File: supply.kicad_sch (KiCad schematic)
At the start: 0 parts

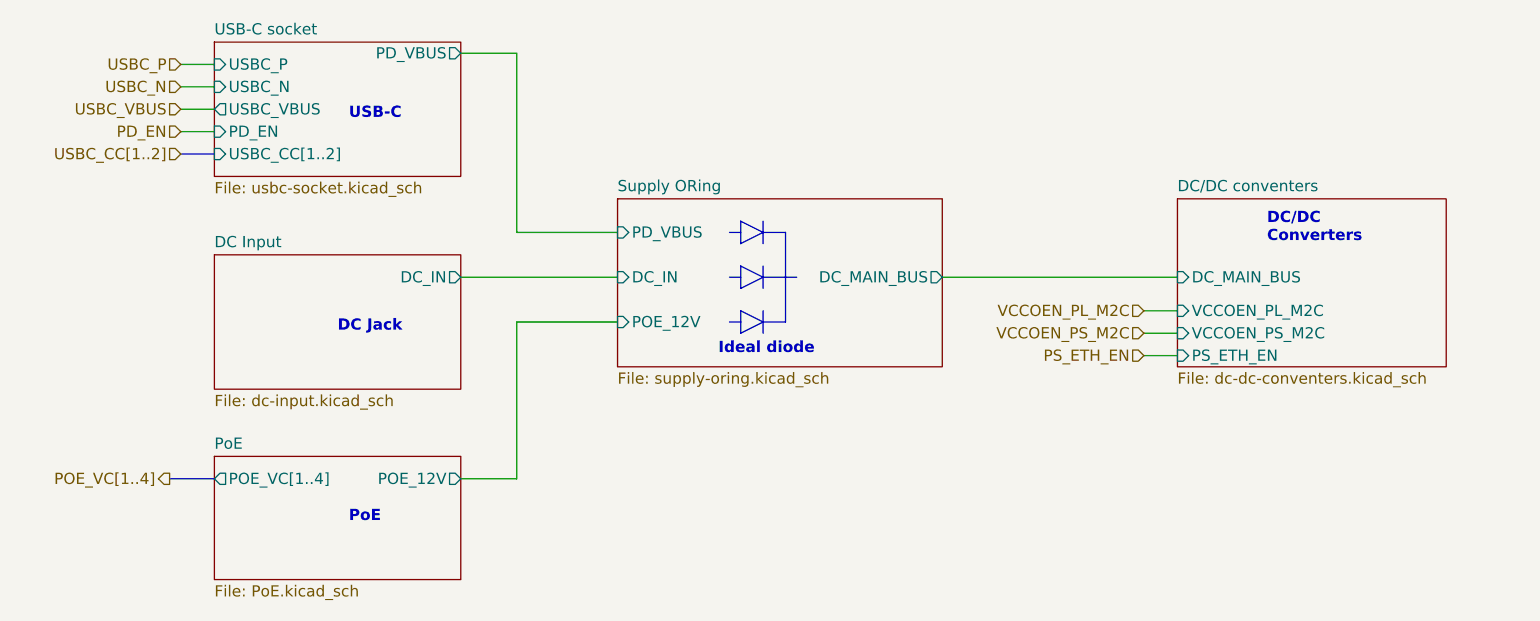
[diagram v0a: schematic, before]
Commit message: removed PoE from schematic
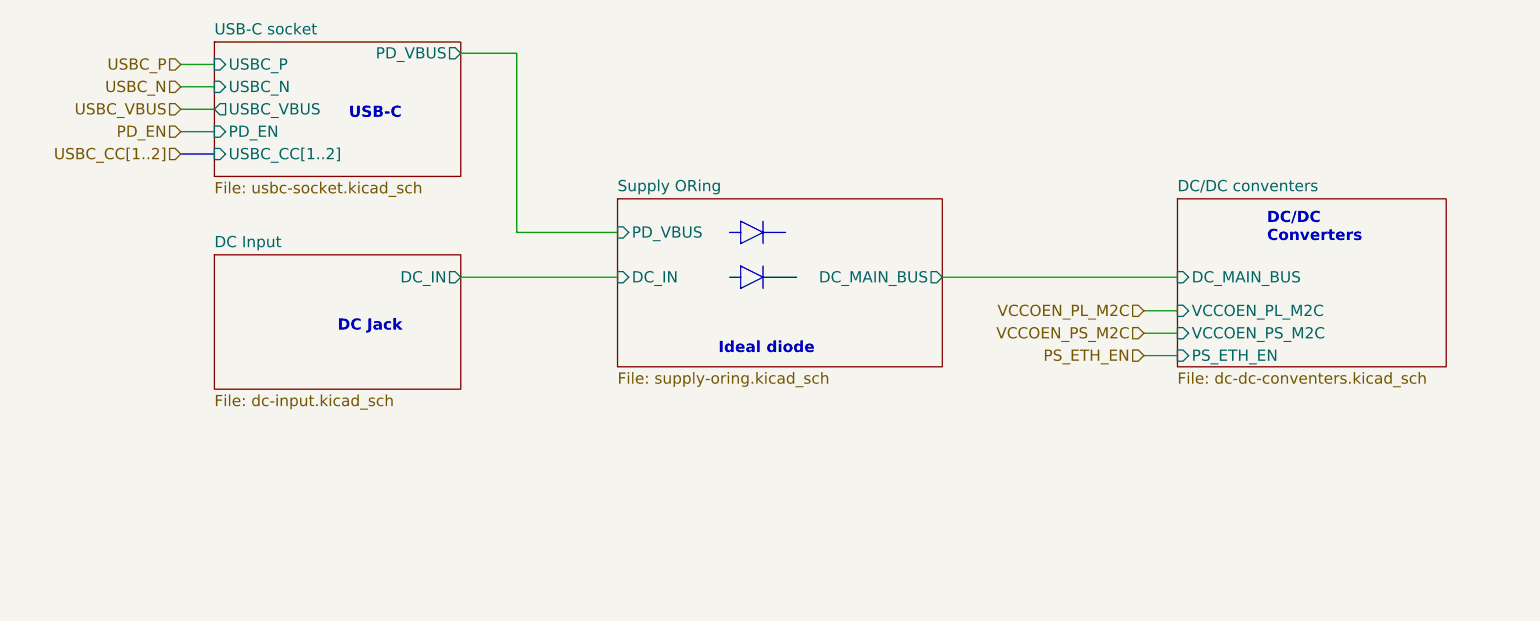
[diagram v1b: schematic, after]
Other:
- removed sheet PoE
- sheet Supply ORing ports: added none; removed POE_12V
- note removed: "PoE"
